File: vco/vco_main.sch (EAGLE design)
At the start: 101 parts, among them IC1 OPA4130U, IC2 LM13700M, IC3 OPA4130U, IC4 OPA4130U, Q1 MMBFJ3

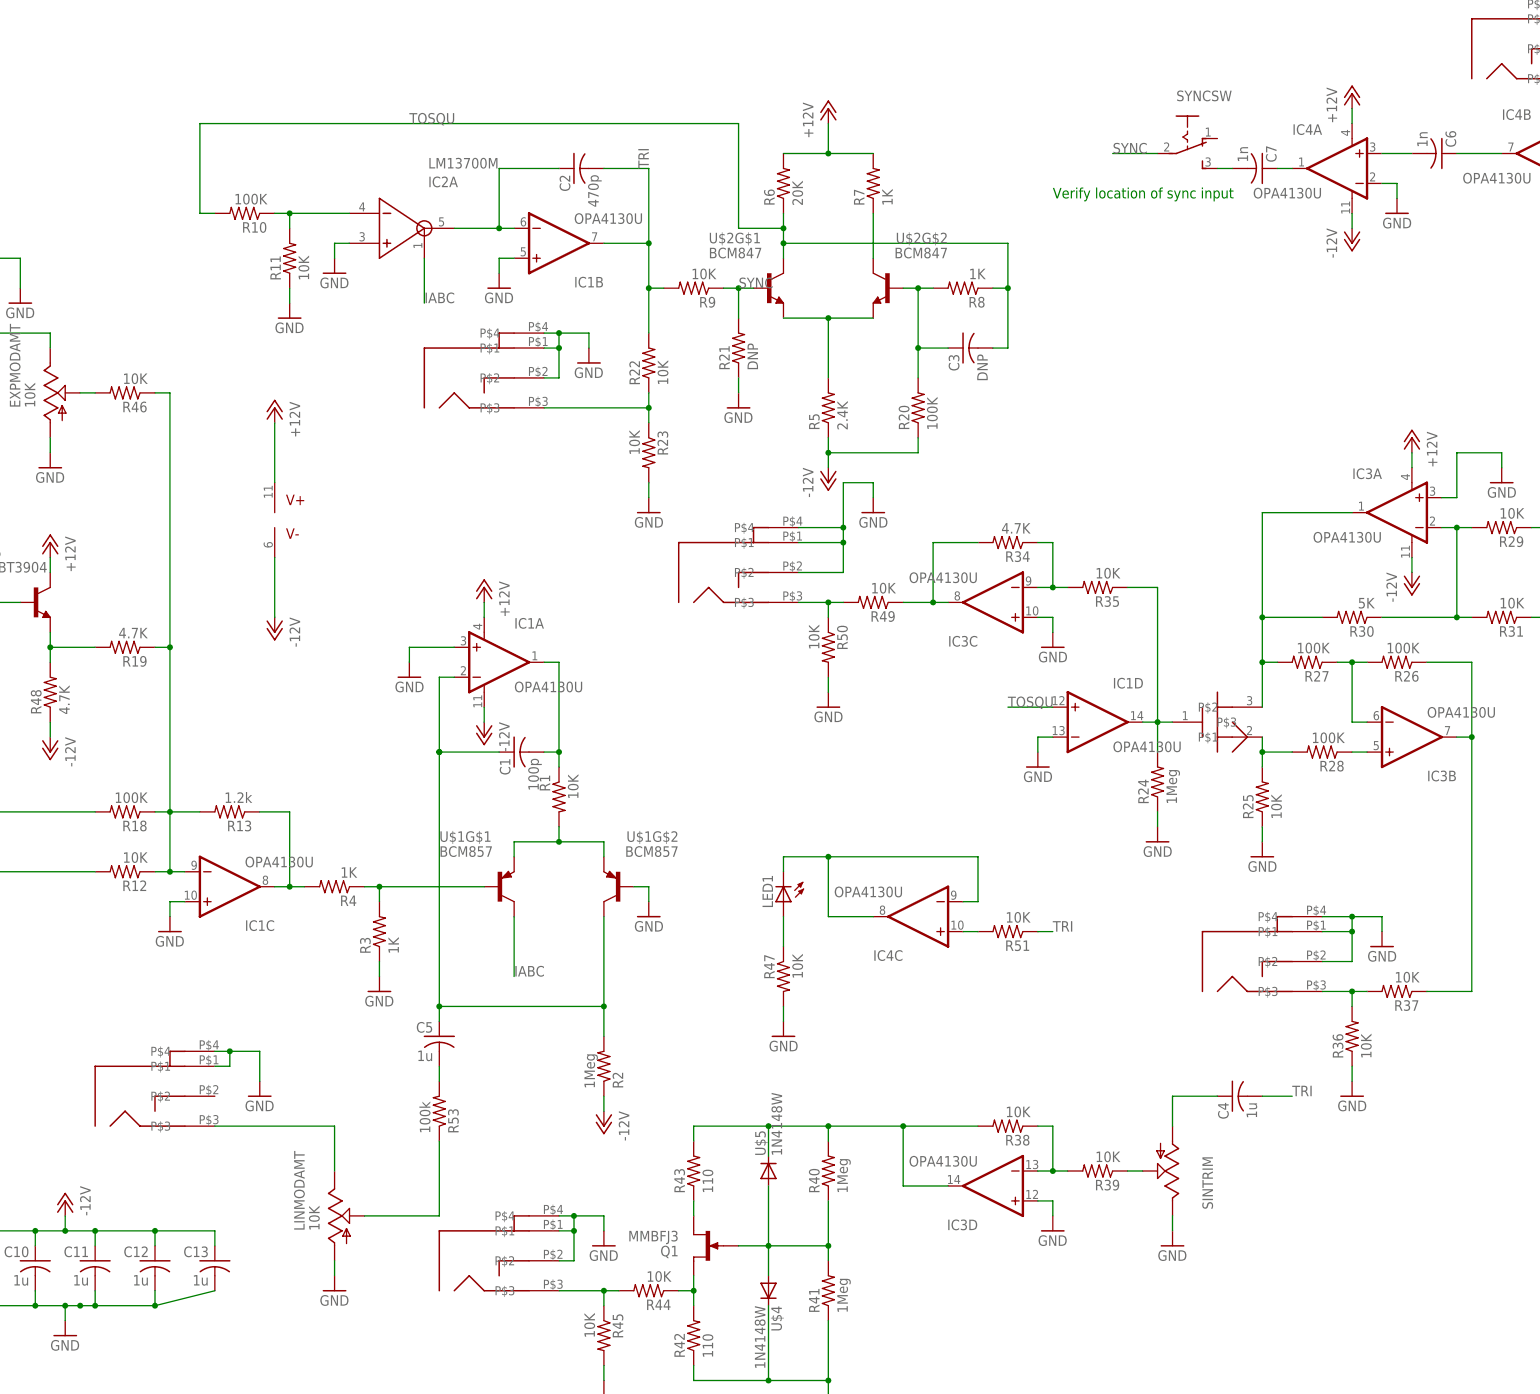
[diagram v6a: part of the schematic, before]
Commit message: finished er up.  ordered 2nd rev of pcb and 1st rev of front panel.
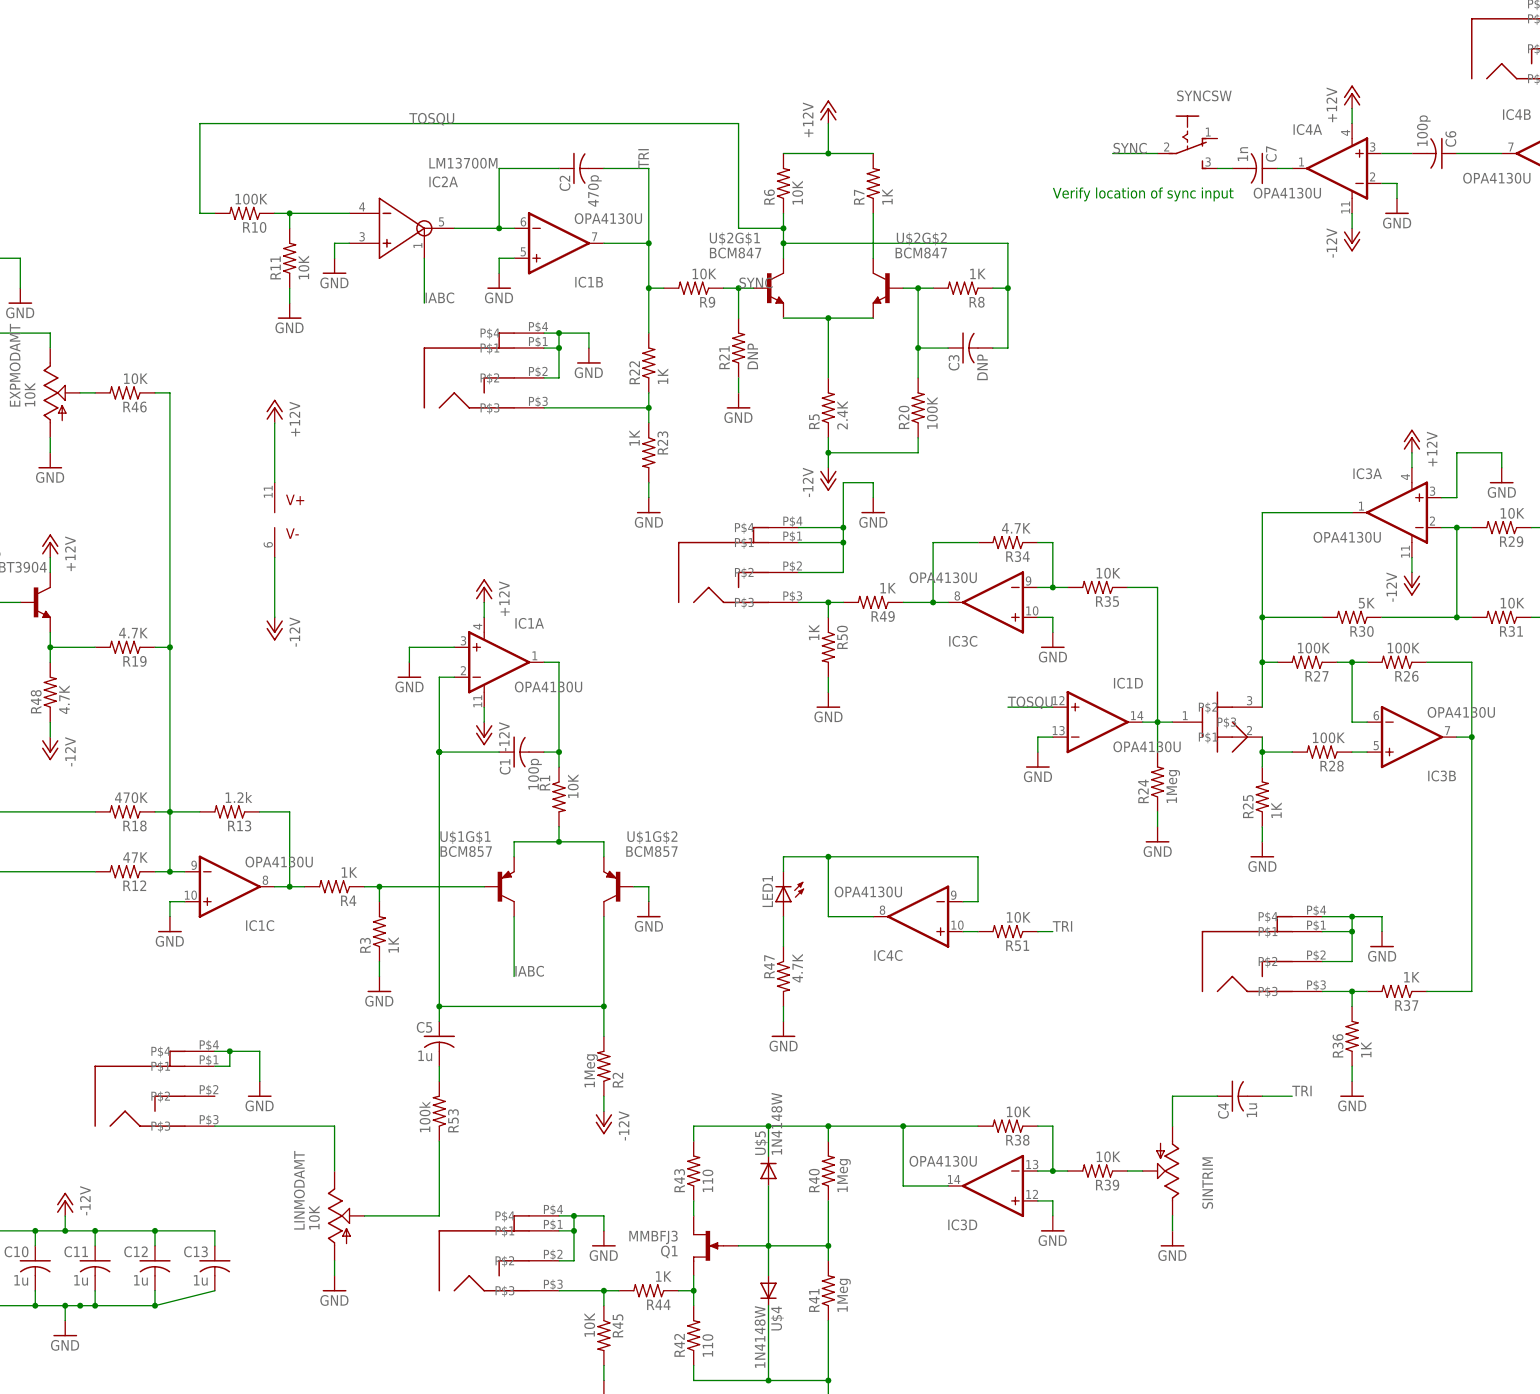
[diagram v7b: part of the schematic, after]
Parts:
- C6: value 1n -> 100p
- R12: value 10K -> 47K
- R18: value 100K -> 470K
- R22, R23, R25, R36, R37, R44, R49, R50: value 10K -> 1K
- R47: value 10K -> 4.7K
- R6: value 20K -> 10K
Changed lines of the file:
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@@
 <part name="U$2" library="dan" deviceset="BCM847" device=""/>
 <part name="R5" library="dan" deviceset="R-US_" device="R0603" value="2.4K"/>
-<part name="R6" library="dan" deviceset="R-US_" device="R0603" value="20K"/>
+<part name="R6" library="dan" deviceset="R-US_" device="R0603" value="10K"/>
 <part name="R7" library="dan" deviceset="R-US_" device="R0603" value="1K"/>
 <part name="P+3" library="dan" deviceset="+12V" device=""/>
@@
 <part name="GND4" library="dan" deviceset="GND" device=""/>
 <part name="GND5" library="dan" deviceset="GND" device=""/>
-<part name="R12" library="dan" deviceset="R-US_" device="R0603" value="10K"/>
+<part name="R12" library="dan" deviceset="R-US_" device="R0603" value="47K"/>
 <part name="R13" library="dan" deviceset="R-US_" device="R0603" value="1.2k"/>
 <part name="GND6" library="dan" deviceset="GND" device=""/>
@@
 <part name="P-4" library="dan" deviceset="-12V" device=""/>
 <part name="P+2" library="dan" deviceset="+12V" device=""/>
-<part name="R18" library="dan" deviceset="R-US_" device="R0603" value="100K"/>
+<part name="R18" library="dan" deviceset="R-US_" device="R0603" value="470K"/>
 <part name="R19" library="dan" deviceset="R-US_" device="R0603" value="4.7K"/>
 <part name="P-5" library="dan" deviceset="-12V" device=""/>
@@
 <part name="TRIOUT" library="dan" deviceset="PJ301BM" device=""/>
 <part name="GND11" library="dan" deviceset="GND" device=""/>
-<part name="R22" library="dan" deviceset="R-US_" device="R0603" value="10K"/>
-<part name="R23" library="dan" deviceset="R-US_" device="R0603" value="10K"/>
+<part name="R22" library="dan" deviceset="R-US_" device="R0603" value="1K"/>
+<part name="R23" library="dan" deviceset="R-US_" device="R0603" value="1K"/>
 <part name="GND12" library="dan" deviceset="GND" device=""/>
 <part name="GND13" library="dan" deviceset="GND" device=""/>
@@
 <part name="R24" library="dan" deviceset="R-US_" device="R0603" value="1Meg"/>
 <part name="GND14" library="dan" deviceset="GND" device=""/>
-<part name="R25" library="dan" deviceset="R-US_" device="R0603" value="10K"/>
+<part name="R25" library="dan" deviceset="R-US_" device="R0603" value="1K"/>
 <part name="GND15" library="dan" deviceset="GND" device=""/>
 <part name="IC3" library="dan" deviceset="OPA4130" device="U"/>
@@
 <part name="GND18" library="dan" deviceset="GND" device=""/>
 <part name="SAW" library="dan" deviceset="PJ301BM" device=""/>
-<part name="R36" library="dan" deviceset="R-US_" device="R0603" value="10K"/>
-<part name="R37" library="dan" deviceset="R-US_" device="R0603" value="10K"/>
+<part name="R36" library="dan" deviceset="R-US_" device="R0603" value="1K"/>
+<part name="R37" library="dan" deviceset="R-US_" device="R0603" value="1K"/>
 <part name="GND19" library="dan" deviceset="GND" device=""/>
 <part name="GND20" library="dan" deviceset="GND" device=""/>
@@
 <part name="SIN" library="dan" deviceset="PJ301BM" device=""/>
 <part name="GND24" library="dan" deviceset="GND" device=""/>
-<part name="R44" library="dan" deviceset="R-US_" device="R0603" value="10K"/>
+<part name="R44" library="dan" deviceset="R-US_" device="R0603" value="1K"/>
 <part name="R45" library="dan" deviceset="R-US_" device="R0603" value="10K"/>
 <part name="GND25" library="dan" deviceset="GND" device=""/>
@@
 <part name="SYNC" library="dan" deviceset="PJ301BM" device=""/>
 <part name="IC4" library="dan" deviceset="OPA4130" device="U"/>
-<part name="C6" library="dan" deviceset="C-US" device="C0603" value="1n"/>
+<part name="C6" library="dan" deviceset="C-US" device="C0603" value="100p"/>
 <part name="C7" library="dan" deviceset="C-US" device="C0603" value="1n"/>
 <part name="GND29" library="dan" deviceset="GND" device=""/>
@@
 <part name="GND31" library="dan" deviceset="GND" device=""/>
 <part name="SYNCSW" library="dan" deviceset="255SB" device=""/>
-<part name="R47" library="dan" deviceset="R-US_" device="R0603" value="10K"/>
+<part name="R47" library="dan" deviceset="R-US_" device="R0603" value="4.7K"/>
 <part name="GND32" library="dan" deviceset="GND" device=""/>
 <part name="POWER" library="dan" deviceset="2516-" device=""/>
@@
 <part name="P+11" library="dan" deviceset="+12V" device=""/>
 <part name="P-12" library="dan" deviceset="-12V" device=""/>
-<part name="R49" library="dan" deviceset="R-US_" device="R0603" value="10K"/>
-<part name="R50" library="dan" deviceset="R-US_" device="R0603" value="10K"/>
+<part name="R49" library="dan" deviceset="R-US_" device="R0603" value="1K"/>
+<part name="R50" library="dan" deviceset="R-US_" device="R0603" value="1K"/>
 <part name="GND36" library="dan" deviceset="GND" device=""/>
 <part name="R51" library="dan" deviceset="R-US_" device="R0603" value="10K"/>
